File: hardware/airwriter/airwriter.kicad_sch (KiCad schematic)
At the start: 57 parts, among them J1 USB-C 5V in, J2 Mini-DIN-8 to printer, J3 Bring-up USB/UART, J4 Mini-DIN-8 LocalTalk, J5 ICSP, J6 I2C / Qwiic, SW1 CONFIG/BOOT, SW2 MODE/TEST, U1 ESP32-S3-WROOM-1-N8R2, U2 MAX3490ESA+, U3 MAX3232ESE+, U4 AP7361C-33E, U5 USBLC6-2SC6, U6 SP3485EN-L, U7 PIC12F1840-I/SN, U8 SP3485EN-L

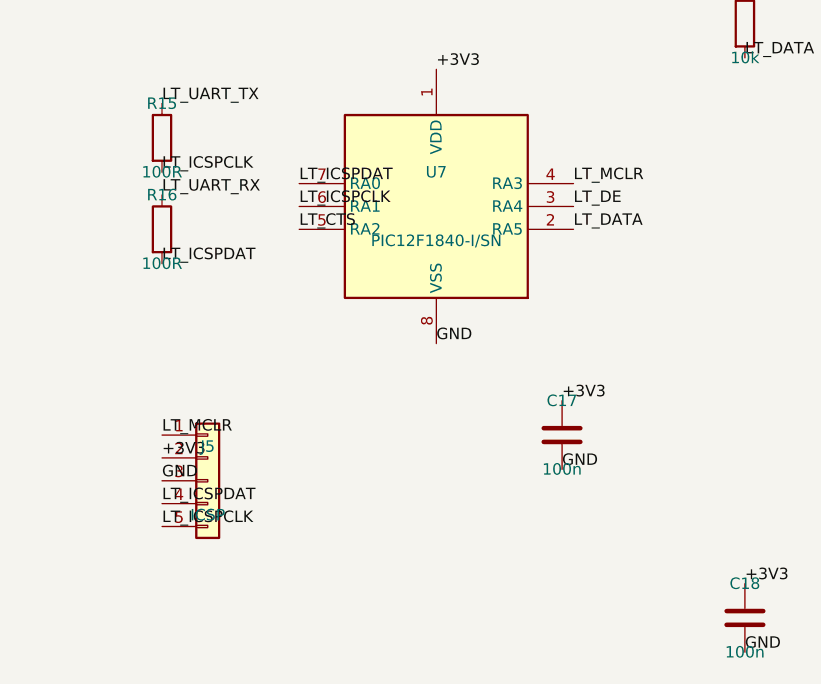
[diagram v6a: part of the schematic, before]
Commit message: Socket the PIC and drop the ICSP header
U7 becomes a PIC12F1840-I/P in PDIP-8, seated in an 8-pin DIP socket, and J5 goes
away. TashTalk gets flashed in a chip programmer before the part is inserted, so a
PIC that will not take firmware never gets soldered down and there is no header
that exists purely for a one-time factory step.

MCLR now ties to +3V3. It was only ever wired to J5 pin 1, so with no programmer
attached it was floating -- held up by nothing but the PIC's internal weak pull-up.
There is no in-circuit programming left to protect, so no series resistor. This does
give up TashTalk's reset-and-tristate feature, which only matters when something
else shares the RS-422 driver; nothing here does. Run MCLR to a spare GPIO if that
ever changes.

The socket is 10.7 x 10.8mm against the SOIC-8's 7.8 x 4.9, so the top-right block
spread out: U7 centres on (133.5, 69), C17/R14/R18/R19 moved right to x=141.5, and
R15/R16 dropped to y=76. Watch the DIP-8 footprint origin -- it is pad 1, not the
body centre, offset 3.81mm in both axes.

The socket is not a BOM line, because kicad-cli only emits parts with a schematic
symbol and the socket is a footprint, not a part. Buy it separately: LCSC C72124,
$0.024. U7's BOM description says so. The PIC itself moves to Mouser or Digi-Key --
LCSC stocks only the SOIC.

J6 is now labelled I2C DISPLAY, which is what the port is actually for.

Also: "schematic parity clean" in the handoff was never verified. kicad-cli only
runs that check with --schematic-parity and no earlier run passed it. The real count
is 15, was 16, and the one that went away was J5's. All of them are field-text
mismatches, the four mounting holes having no symbol, and net conflicts on pads that
are genuinely unconnected. No wiring errors. Corrected the claim.

Re-routed and re-stitched: 61 stitching vias, 6 pour fragments unjoined. DRC is down
to a single violation, the known U1 library mismatch from its 0.30mm vias. ERC
unchanged at four pre-existing warnin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
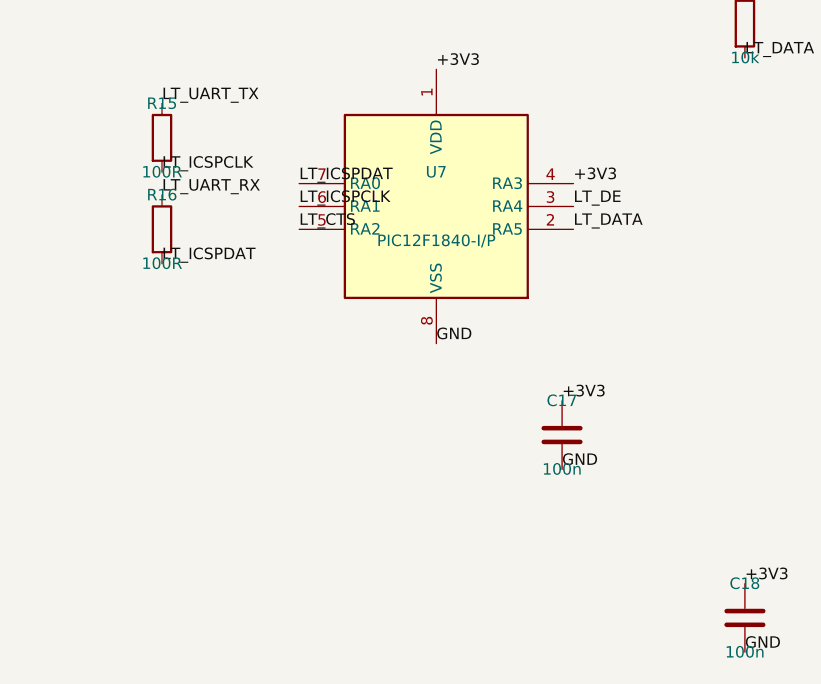
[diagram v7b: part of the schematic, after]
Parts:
- removed J5: ICSP, Connector_PinHeader_1.27mm:PinHeader_1x05_P1.27mm_Vertical, symbol Connector_Generic:Conn_01x05
- U7: value PIC12F1840-I/SN -> PIC12F1840-I/P; footprint Package_SO:SOIC-8_3.9x4.9mm_P1.27mm -> Package_DIP:DIP-8_W7.62mm_Socket; MPN PIC12F1840-I/SN -> PIC12F1840-I/P
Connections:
- net LT_MCLR is gone; now on net +3V3: U7.4 (RA3)
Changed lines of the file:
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@@
-      (justify left bottom))
-)
-  (label "LT_ICSPCLK"
-    (at 240.03 265.43 0)
-    (effects
-      (font
-        (size 1.27 1.27))
       (justify left bottom))
 )
@@
       (justify left bottom))
 )
-  (label "LT_ICSPDAT"
-    (at 240.03 262.89 0)
-    (effects
-      (font
-        (size 1.27 1.27))
-      (justify left bottom))
-)
   (label "LT_CTS"
     (at 189.23 137.16 0)
@@
       (justify left bottom))
 )
-  (label "LT_MCLR"
+  (label "+3V3"
     (at 285.75 227.33 0)
-    (effects
-      (font
-        (size 1.27 1.27))
-      (justify left bottom))
-)
-  (label "LT_MCLR"
-    (at 240.03 255.27 0)
     (effects
       (font
@@
       (justify left bottom))
 )
-  (label "+3V3"
-    (at 240.03 257.81 0)
-    (effects
-      (font
-        (size 1.27 1.27))
-      (justify left bottom))
-)
   (label "GND"
     (at 270.51 245.11 0)
@@
   (label "GND"
     (at 284.48 259.08 0)
-    (effects
-      (font
-        (size 1.27 1.27))
-      (justify left bottom))
-)
-  (label "GND"
-    (at 240.03 260.35 0)
     (effects
       (font
@@
         (font
           (size 1.27 1.27))))
-    (property "Value" "PIC12F1840-I/SN"
+    (property "Value" "PIC12F1840-I/P"
       (at 270.51 233.68 0)
       (effects
         (font
           (size 1.27 1.27))))
-    (property "Footprint" "Package_SO:SOIC-8_3.9x4.9mm_P1.27mm"
+    (property "Footprint" "Package_DIP:DIP-8_W7.62mm_Socket"
       (at 270.51 229.87 0)
       (hide yes)
@@
         (font
           (size 1.27 1.27))))
-    (property "MPN" "PIC12F1840-I/SN"
+    (property "MPN" "PIC12F1840-I/P"
       (at 270.51 229.87 0)
       (hide yes)
@@
         (font
           (size 1.27 1.27))))
-    (property "Description" "8-bit MCU, SOIC-8, runs TashTalk LocalTalk firmware"
+    (property "Description" "8-bit MCU, PDIP-8 in an 8-pin DIP socket. Runs TashTalk. Program it in a chip programmer before inserting - there is no ICSP header"
       (at 270.51 229.87 0)
       (hide yes)
@@
           (unit 1)))))
   (symbol
-    (lib_id "Connector_Generic:Conn_01x05")
-    (at 245.11 260.35 0)
-    (unit 1)
-    (in_bom yes)
-    (on_board yes)
-    (dnp no)
-    (property "Reference" "J5"
-      (at 245.11 256.54 0)
-      (effects
-        (font
-          (size 1.27 1.27))))
-    (property "Value" "ICSP"
-      (at 245.11 264.16 0)
-      (effects
-        (font
-          (size 1.27 1.27))))
-    (property "Footprint" "Connector_PinHeader_1.27mm:PinHeader_1x05_P1.27mm_Vertical"
-      (at 245.11 260.35 0)
-      (hide yes)
-      (effects
-        (font
-          (size 1.27 1.27))))
-    (property "MPN" ""
-      (at 245.11 260.35 0)
-      (hide yes)
-      (effects
-        (font
-          (size 1.27 1.27))))
-    (property "Manufacturer" "Any"
-      (at 245.11 260.35 0)
-      (hide yes)
-      (effects
-        (font
-          (size 1.27 1.27))))
-    (property "Description" "1x5 1.27mm pin header, ICSP for the PIC"
-      (at 245.11 260.35 0)
-      (hide yes)
-      (effects
-        (font
-          (size 1.27 1.27))))
-    (property "Datasheet" ""
-      (at 245.11 260.35 0)
-      (hide yes)
-      (effects
-        (font
-          (size 1.27 1.27))))
-    (instances
-      (project "airwriter"
-        (path "/b907fa76-c5fe-4a7a-8e4e-adfdab62cb9c"
-          (reference "J5")
-          (unit 1)))))
-  (symbol

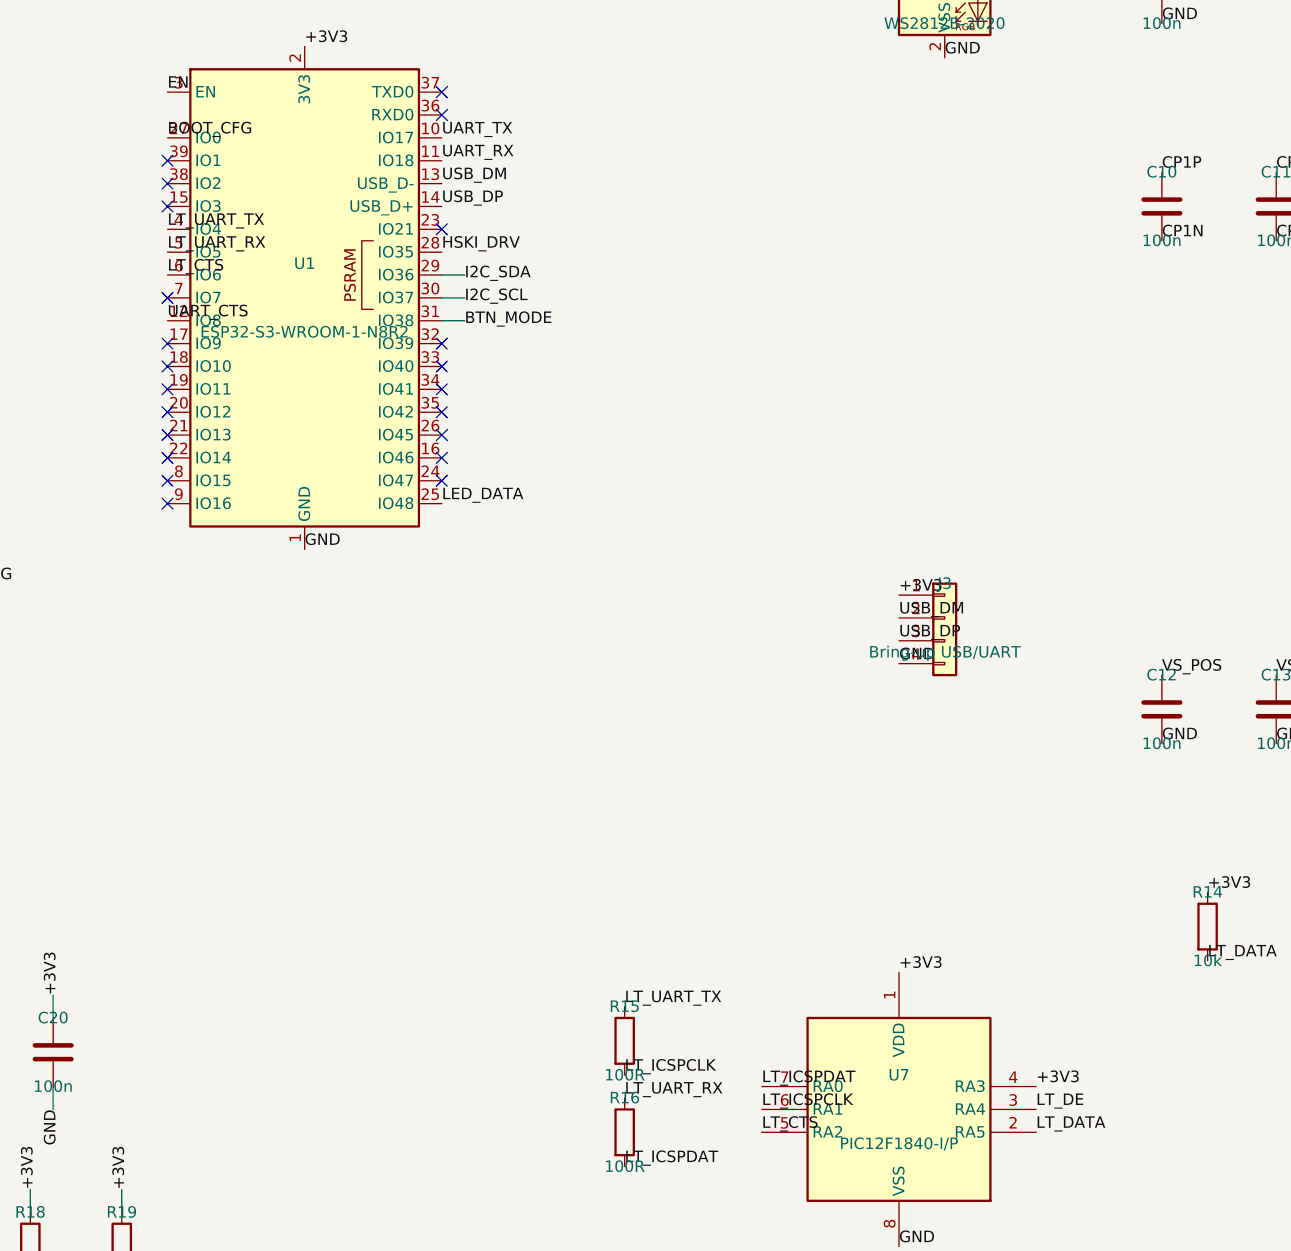
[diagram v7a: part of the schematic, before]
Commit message: Give firmware a reset line to the LocalTalk chip
MCLR on U7 was tied to +3V3, which is safe but leaves the PIC restartable only by
unplugging the board. It now runs to the ESP32 on IO2 as net LT_RESET.

This is worth having on a headless dongle. Firmware can recover a wedged TashTalk
without a power cycle, and can hold the PIC in reset in the modes where LocalTalk is
not the live transport. Driving the GPIO low asserts reset; leaving it an input --
which is what it is through ESP32 boot -- lets the PIC's internal pull-up on MCLR
run the chip. No external resistor needed.

IO2 was chosen because it is a plain GPIO, not a strapping pin, not JTAG and not the
boot console UART, and because it is the nearest free module pad to U7 at 5.1mm.

The wire costs nothing at fab and cannot be added after the boards exist, so it goes
in before the order rather than after the first bug.

Re-routed and re-stitched: 50 stitching vias, 7 pour fragments unjoined. DRC still a
single known violation, ERC still four pre-existing warnings, parity unchanged at 15.
Drill floor 0.300mm. Fab package regenerated.
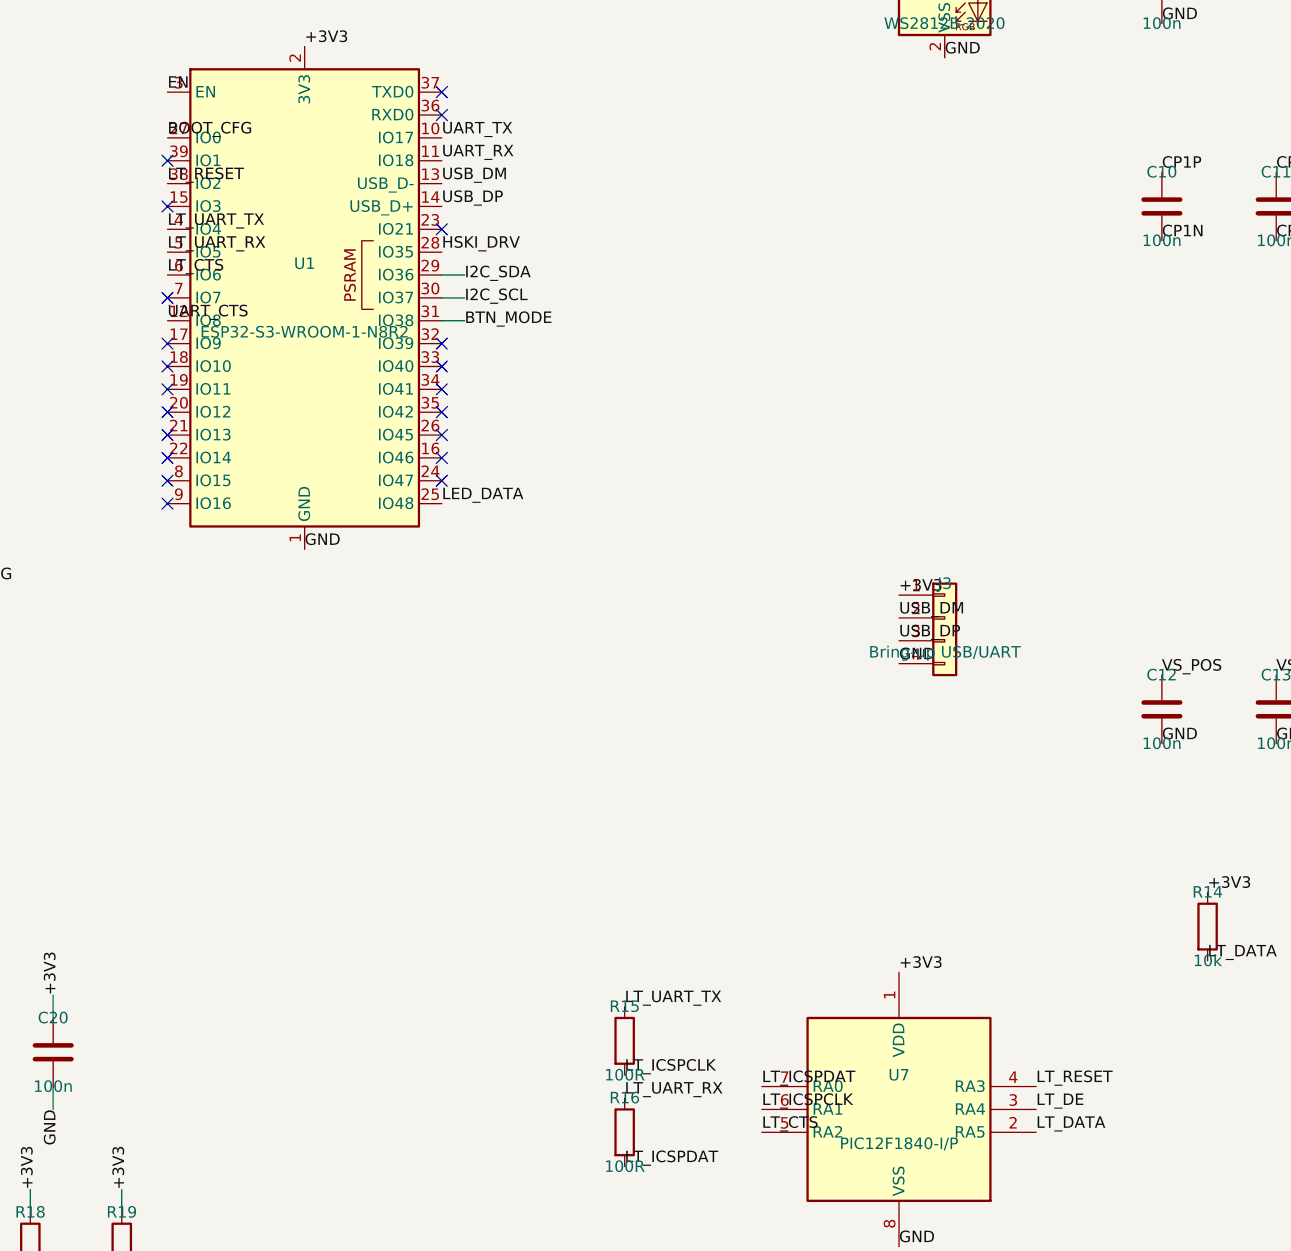
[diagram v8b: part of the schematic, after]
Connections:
- net +3V3: no longer U7.4 (RA3)
- net LT_RESET: now reaches U1.38 (IO2)
- net LT_RESET: now also U7.4 (RA3)
- no-connect marks 40 -> 39
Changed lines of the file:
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@@
     (at 189.23 124.46)
 )
-  (no_connect
-    (at 189.23 127)
+  (label "LT_RESET"
+    (at 189.23 127 0)
+    (effects
+      (font
+        (size 1.27 1.27))
+      (justify left bottom))
 )
   (no_connect
@@
       (justify left bottom))
 )
-  (label "+3V3"
+  (label "LT_RESET"
     (at 285.75 227.33 0)
     (effects
